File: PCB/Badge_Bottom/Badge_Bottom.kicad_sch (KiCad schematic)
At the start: 10 parts, among them CN1 PJ-320, CN2 PJ-320, J1 USB_C_Receptacle_USB2.0, J3 Conn_01x01_Pin, Q1 AO3400A, SW1 TM-2024A, SW2 TM-2024A, U2 CH32V305RBT6

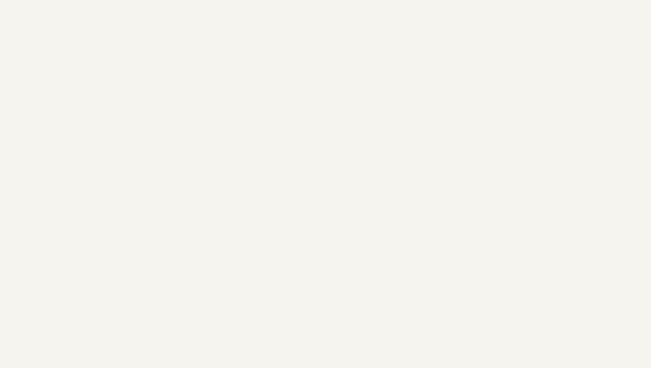
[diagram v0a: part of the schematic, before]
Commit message: Added todo for bottom badge
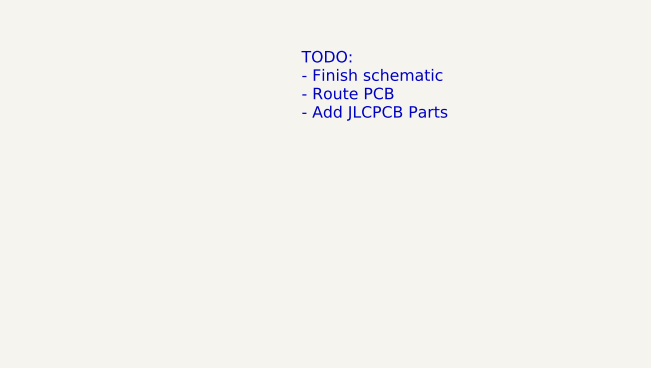
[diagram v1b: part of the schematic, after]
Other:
- note added: "TODO: - Finish schematic - Route PCB - Add JLCPCB Parts"
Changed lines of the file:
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@@
     (stroke (width 0) (type default))
+  )
+  (text "TODO:\n- Finish schematic\n- Route PCB\n- Add JLCPCB Parts"
+    (at 204.47 36.83 0)
+    (effects (font (size 1.27 1.27)) (justify left bottom))
   )
   (symbol (lib_id "Connector:USB_C_Receptacle_USB2.0") (at 50.8 99.06 0) (unit 1)

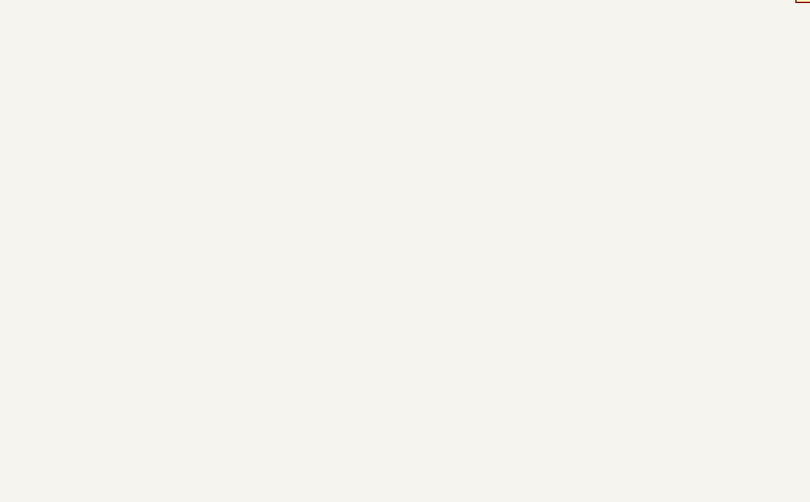
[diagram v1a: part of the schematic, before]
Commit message: Added pcb outline from Badge_Top, added todos in pcb file
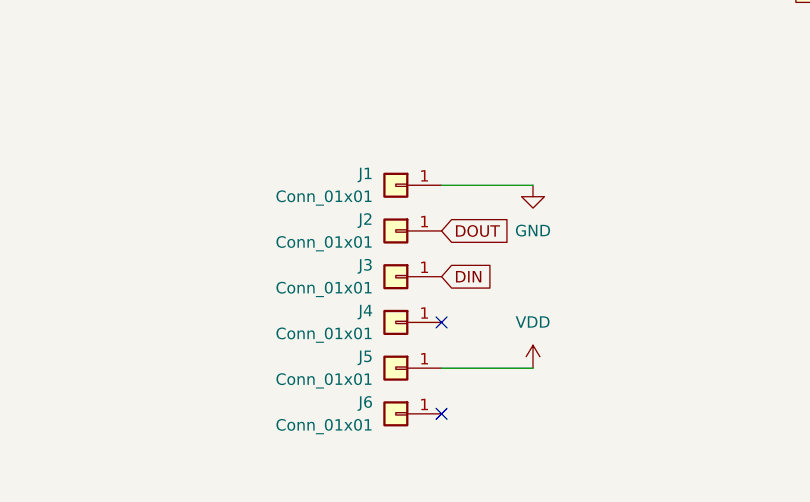
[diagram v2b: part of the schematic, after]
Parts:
- added J1, J2, J3, J4, J5, J6: Conn_01x01, Mounting_Wuerth:Mounting_Wuerth_WA-SMSI-M2_H7mm_9774070243, symbol Connector_Generic:Conn_01x01
- CN1, CN2: footprint kicad:AUDIO-TH_HOOYA_PJ-320 -> PJ-320:AUDIO-TH_HOOYA_PJ-320
- J1: footprint (none) -> Connector_USB:USB_C_Receptacle_HRO_TYPE-C-31-M-12
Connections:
- net GND: now also J1.1 (Pin_1)
- new net DIN: J3.1 (Pin_1)
- new net DOUT: J2.1 (Pin_1)
- new net VDD: J5.1 (Pin_1)
- no-connect marks 0 -> 2

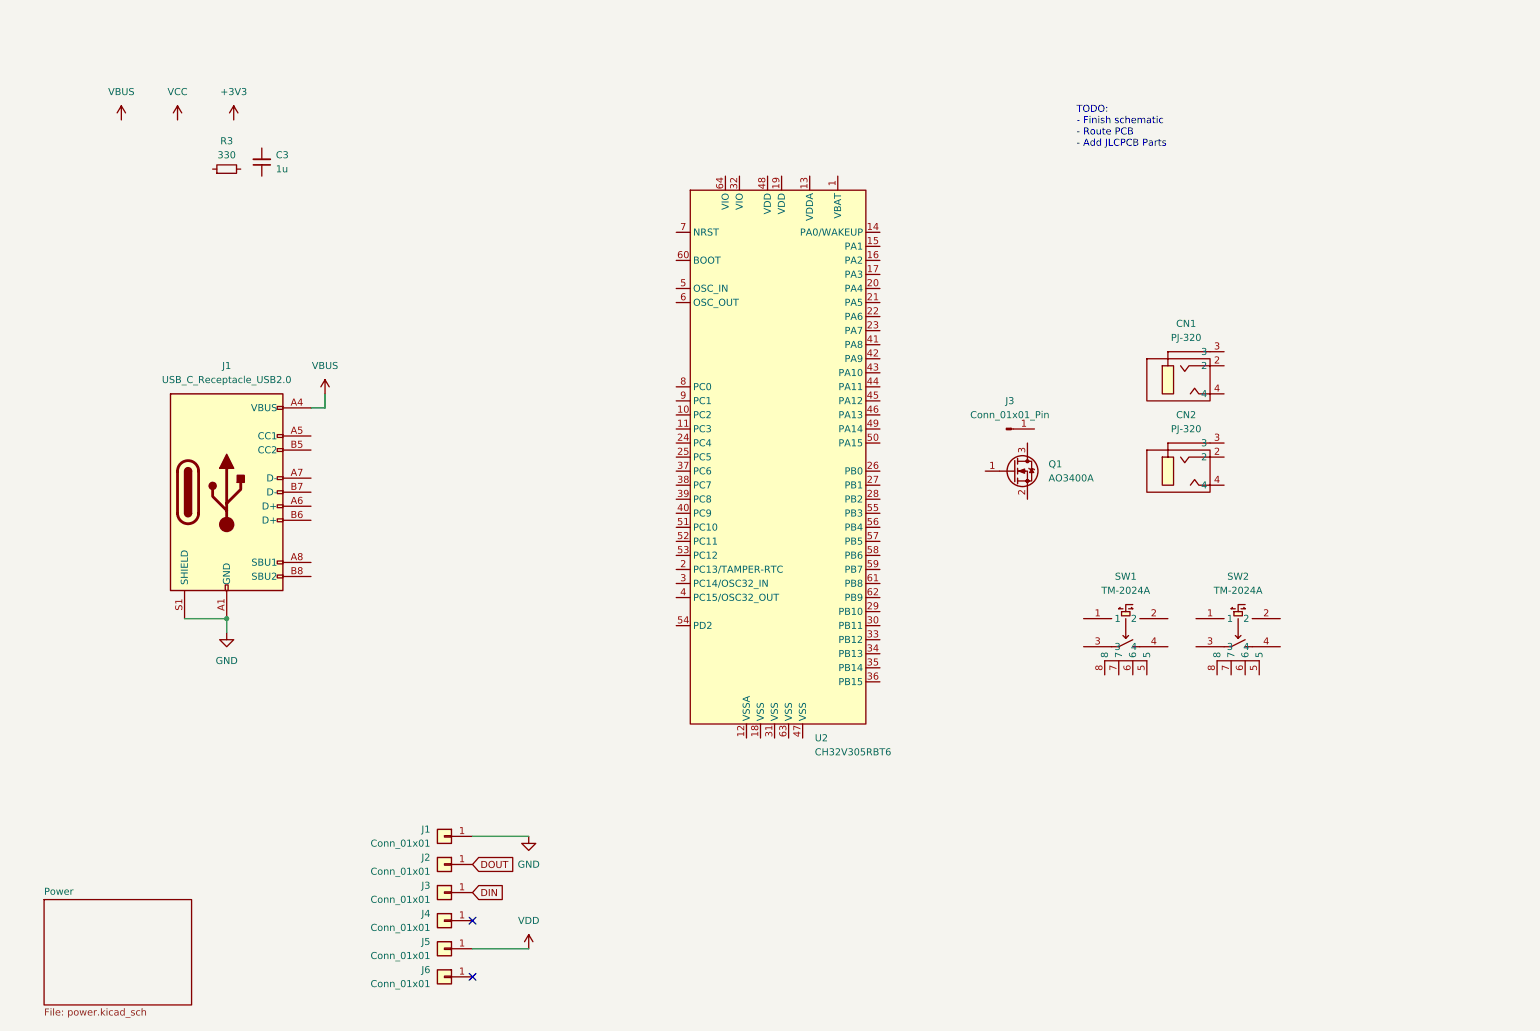
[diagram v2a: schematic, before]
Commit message: Added new page for IO, added new components, added JLC parts, fixed PCB standoffs to be pads and modified concept of PCB (dual usbc)
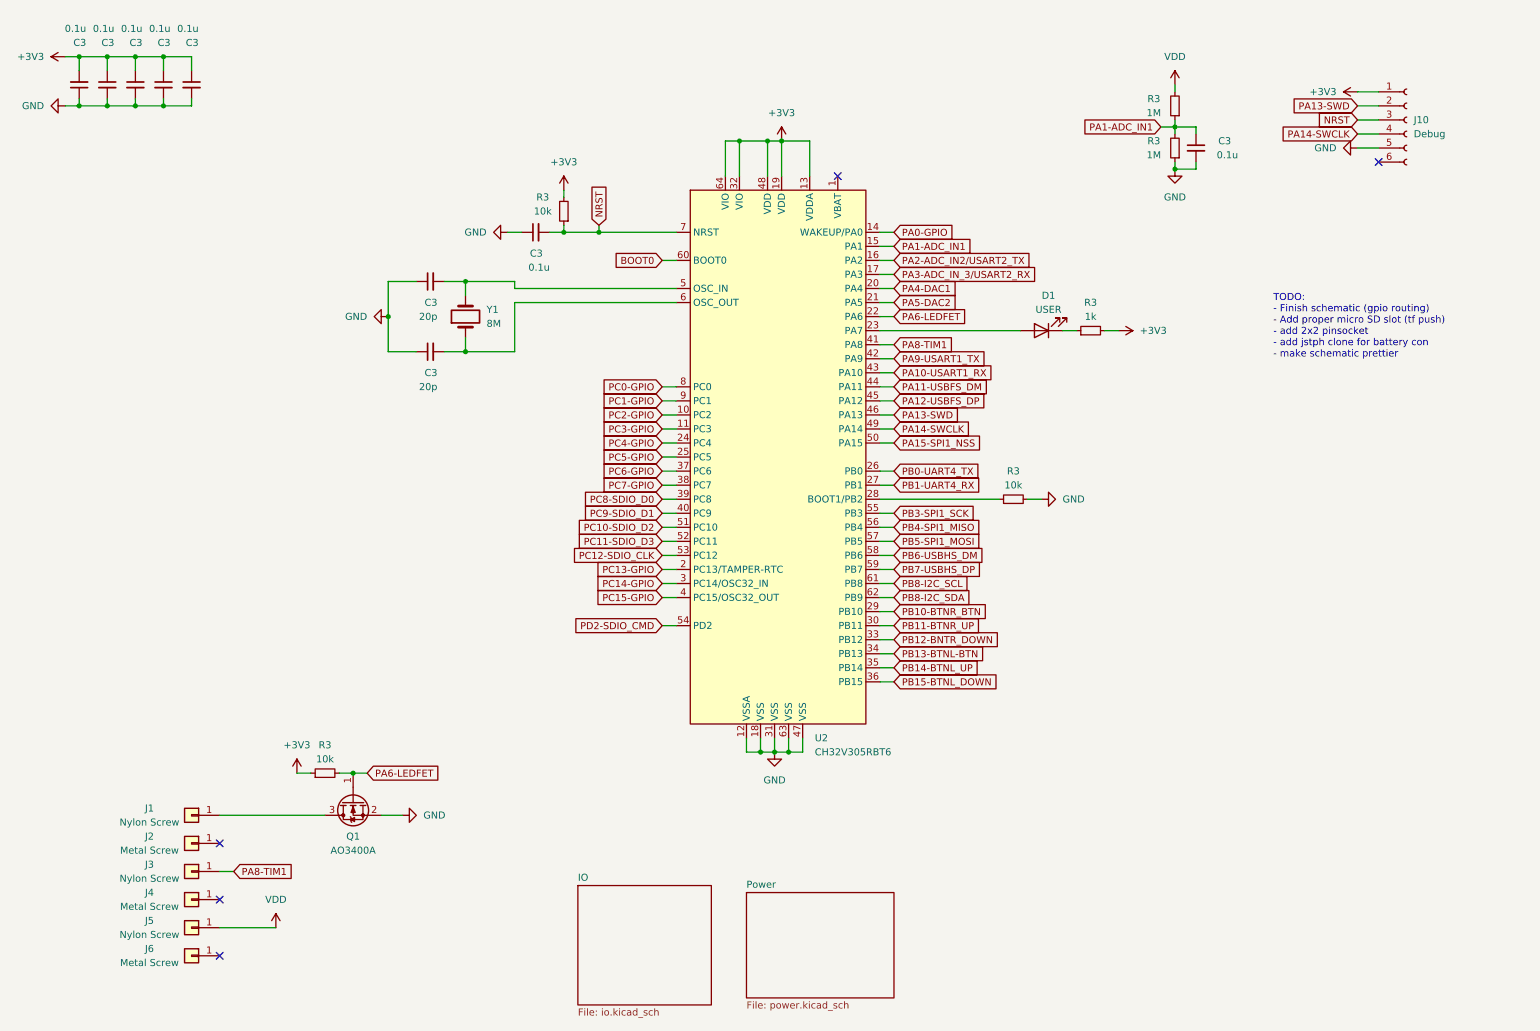
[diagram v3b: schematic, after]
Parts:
- removed CN1, CN2: PJ-320, PJ-320:AUDIO-TH_HOOYA_PJ-320, symbol PJ-320:PJ-320
- removed J1: USB_C_Receptacle_USB2.0, Connector_USB:USB_C_Receptacle_HRO_TYPE-C-31-M-12, symbol Connector:USB_C_Receptacle_USB2.0
- removed J3: Conn_01x01_Pin, Connector_Wire:SolderWirePad_1x01_SMD_1x2mm, symbol Connector:Conn_01x01_Pin
- removed SW1, SW2: TM-2024A, TM2024A:SW-SMD_TM-2024A, symbol TM2024A:TM-2024A
- added C3 (x6): 0.1u, Capacitor_SMD:C_0603_1608Metric, symbol Device:C_Small
- added C3 (x2): 20p, Capacitor_SMD:C_0603_1608Metric, symbol Device:C_Small
- added D1: USER, LED_SMD:LED_0603_1608Metric, symbol Device:LED
- added J10: Debug, Paw-Connect_RevB_TC2030-IDC-NL_2x03_P1.27mm_Vertical:Paw-Connect_RevB_TC2030-IDC-NL_2x03_P1.27mm_Vertical, symbol Connector:Conn_01x06_Socket
- added R3 (x2): 10k, Resistor_SMD:R_0603_1608Metric, symbol Device:R_Small
- added R3 (x2): 1M, Resistor_SMD:R_0603_1608Metric, symbol Device:R_Small
- added R3: 1k, Resistor_SMD:R_0603_1608Metric, symbol Device:R_Small
- added Y1: 8M, Crystal:Crystal_SMD_5032-2Pin_5.0x3.2mm, symbol Device:Crystal
- C3: value 1u -> 0.1u; footprint (none) -> Capacitor_SMD:C_0603_1608Metric
- J1, J3, J5: value Conn_01x01 -> Nylon Screw; footprint Mounting_Wuerth:Mounting_Wuerth_WA-SMSI-M2_H7mm_9774070243 -> standoff_pad_m2:Standoff_Pad_M2
- J2, J4, J6: value Conn_01x01 -> Metal Screw; footprint Mounting_Wuerth:Mounting_Wuerth_WA-SMSI-M2_H7mm_9774070243 -> standoff_pad_m2:Standoff_Pad_M2
- R3: value 330 -> 10k; footprint (none) -> Resistor_SMD:R_0603_1608Metric
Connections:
- net DIN is gone; now on net PA8-TIM1: J3.1 (Pin_1)
- net +3V3: now also C3.1, U2.13 (VDDA), U2.19 (VDD), U2.32 (VIO), U2.48 (VDD), U2.64 (VIO), C3.1, C3.1, C3.1, C3.2, J10.1 (Pin_1), R3.1, R3.2, R3.2
- net GND: now also C3.2, Q1.2 (S), R3.2, U2.12 (VSSA), U2.18 (VSS), U2.31 (VSS), U2.47 (VSS), U2.63 (VSS), C3.1, C3.1, C3.1, C3.1, C3.2, C3.2, C3.2, C3.2, J10.5 (Pin_5), R3.1; no longer J1.1 (Pin_1)
- net VDD: now also R3.2
- net at R3.1: now also U2.28 (BOOT1/PB2)
- net PC2-GPIO: now reaches U2.10 (PC2)
- net PC3-GPIO: now reaches U2.11 (PC3)
- net PA0-GPIO: now reaches U2.14 (WAKEUP/PA0)
- net PA1-ADC_IN1: now reaches U2.15 (PA1)
- net PA1-ADC_IN1: now also C3.1, R3.1, R3.2
- net PA2-ADC_IN2/USART2_TX: now reaches U2.16 (PA2)
- net PA3-ADC_IN_3/USART2_RX: now reaches U2.17 (PA3)
- net PC13-GPIO: now reaches U2.2 (PC13/TAMPER-RTC)
- net PA4-DAC1: now reaches U2.20 (PA4)
- net PA5-DAC2: now reaches U2.21 (PA5)
- net PA6-LEDFET: now reaches U2.22 (PA6)
- net PA6-LEDFET: now also Q1.1 (G), R3.2
- net at U2.23 (PA7): now also D1.2 (A)
- net PC4-GPIO: now reaches U2.24 (PC4)
- net PC5-GPIO: now reaches U2.25 (PC5)
- net PB0-UART4_TX: now reaches U2.26 (PB0)
- net PB1-UART4_RX: now reaches U2.27 (PB1)
- net PB10-BTNR_BTN: now reaches U2.29 (PB10)
- net PC14-GPIO: now reaches U2.3 (PC14/OSC32_IN)
- net PB11-BTNR_UP: now reaches U2.30 (PB11)
- net PB12-BNTR_DOWN: now reaches U2.33 (PB12)
- net PB13-BTNL-BTN: now reaches U2.34 (PB13)
- net PB14-BTNL_UP: now reaches U2.35 (PB14)
- net PB15-BTNL_DOWN: now reaches U2.36 (PB15)
- net PC6-GPIO: now reaches U2.37 (PC6)
- net PC7-GPIO: now reaches U2.38 (PC7)
- net PC8-SDIO_D0: now reaches U2.39 (PC8)
- net PC15-GPIO: now reaches U2.4 (PC15/OSC32_OUT)
- net PC9-SDIO_D1: now reaches U2.40 (PC9)
- net PA8-TIM1: now reaches U2.41 (PA8)
- net PA9-USART1_TX: now reaches U2.42 (PA9)
- net PA10-USART1_RX: now reaches U2.43 (PA10)
- net PA11-USBFS_DM: now reaches U2.44 (PA11)
- net PA12-USBFS_DP: now reaches U2.45 (PA12)
- net PA13-SWD: now reaches U2.46 (PA13)
- net PA13-SWD: now also J10.2 (Pin_2)
- net PA14-SWCLK: now reaches U2.49 (PA14)
- net PA14-SWCLK: now also J10.4 (Pin_4)
- net at U2.5 (OSC_IN): now also C3.2, Y1.2
- net PA15-SPI1_NSS: now reaches U2.50 (PA15)
- net PC10-SDIO_D2: now reaches U2.51 (PC10)
- net PC11-SDIO_D3: now reaches U2.52 (PC11)
- net PC12-SDIO_CLK: now reaches U2.53 (PC12)
- net PD2-SDIO_CMD: now reaches U2.54 (PD2)
- net PB3-SPI1_SCK: now reaches U2.55 (PB3)
- net PB4-SPI1_MISO: now reaches U2.56 (PB4)
- net PB5-SPI1_MOSI: now reaches U2.57 (PB5)
- net PB6-USBHS_DM: now reaches U2.58 (PB6)
- net PB7-USBHS_DP: now reaches U2.59 (PB7)
- net at U2.6 (OSC_OUT): now also C3.2, Y1.1
- net BOOT0: now reaches U2.60 (BOOT0)
- net PB8-I2C_SCL: now reaches U2.61 (PB8)
- net PB8-I2C_SDA: now reaches U2.62 (PB9)
- net NRST: now reaches U2.7 (NRST)
- net NRST: now also C3.2, J10.3 (Pin_3), R3.1
- net PC0-GPIO: now reaches U2.8 (PC0)
- net PC1-GPIO: now reaches U2.9 (PC1)
- net at Q1.3 (D): now also J1.1 (Pin_1)
- net DOUT: no longer names the net of J2.1 (Pin_1)
- new net: D1.1 (K), R3.1
- no-connect marks 2 -> 5
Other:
- added sheet IO (io.kicad_sch)
- note added: "TODO: - Finish schematic (gpio routing) - Add proper micro SD slot (tf push) - add 2x2 pinsocket - add jstph clone for battery con - make schematic prettier"
- note removed: "TODO: - Finish schematic - Route PCB - Add JLCPCB Parts"
- moved on the sheet: C3, J1, J2, J3, J4, J5, J6, Q1, R3

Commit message: finished schematic and added jlc parts
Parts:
- added J18: Debug, Connector_PinSocket_2.54mm:PinSocket_2x02_P2.54mm_Horizontal, symbol Connector_Generic:Conn_02x02_Odd_Even
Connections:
- net GND: now also J18.1 (Pin_1)
- net NRST: now also J18.3 (Pin_3)
- net PA13-SWD: now also J18.2 (Pin_2)
- net PA14-SWCLK: now also J18.4 (Pin_4)
- net PB8-I2C_SDA renamed PB9-I2C_SDA
- net PC13-GPIO renamed PC13-SDIO_CD
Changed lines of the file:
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@@
+    (stroke (width 0) (type default))
+  )
+  (wire (pts (xy 261.62 49.53) (xy 264.16 49.53))
     (stroke (width 0) (type default))
   )
@@
     (stroke (width 0) (type default))
   )
+  (wire (pts (xy 246.38 52.07) (xy 248.92 52.07))
+    (stroke (width 0) (type default))
+  )
   (wire (pts (xy 44.45 29.21) (xy 44.45 27.94))
     (stroke (width 0) (type default))
@@
     (stroke (width 0) (type default))
   )
+  (wire (pts (xy 246.38 49.53) (xy 248.92 49.53))
+    (stroke (width 0) (type default))
+  )
   (wire (pts (xy 21.59 20.32) (xy 24.13 20.32))
     (stroke (width 0) (type default))
@@
   )
   (wire (pts (xy 109.22 52.07) (xy 111.76 52.07))
+    (stroke (width 0) (type default))
+  )
+  (wire (pts (xy 261.62 52.07) (xy 264.16 52.07))
     (stroke (width 0) (type default))
   )
@@
     )
   )
-  (global_label "PB8-I2C_SDA" (shape input) (at 171.45 118.11 0) (fields_autoplaced)
+  (global_label "PB9-I2C_SDA" (shape input) (at 171.45 118.11 0) (fields_autoplaced)
     (effects (font (size 1.27 1.27)) (justify left))
     (property "Intersheetrefs" "${INTERSHEET_REFS}" (at 187.3771 118.11 0)
@@
     )
   )
+  (global_label "NRST" (shape input) (at 246.38 52.07 180) (fields_autoplaced)
+    (effects (font (size 1.27 1.27)) (justify right))
+    (property "Intersheetrefs" "${INTERSHEET_REFS}" (at 238.6172 52.07 0)
+      (effects (font (size 1.27 1.27)) (justify right) hide)
+    )
+  )
   (global_label "PC11-SDIO_D3" (shape input) (at 129.54 107.95 180) (fields_autoplaced)
     (effects (font (size 1.27 1.27)) (justify right))
@@
     )
   )
+  (global_label "PA14-SWCLK" (shape input) (at 264.16 52.07 0) (fields_autoplaced)
+    (effects (font (size 1.27 1.27)) (justify left))
+    (property "Intersheetrefs" "${INTERSHEET_REFS}" (at 279.7242 52.07 0)
+      (effects (font (size 1.27 1.27)) (justify left) hide)
+    )
+  )
   (global_label "PC0-GPIO" (shape input) (at 129.54 80.01 180) (fields_autoplaced)
     (effects (font (size 1.27 1.27)) (justify right))
@@
     )
   )
-  (global_label "PC13-GPIO" (shape input) (at 129.54 113.03 180) (fields_autoplaced)
+  (global_label "PC13-SDIO_CD" (shape input) (at 129.54 113.03 180) (fields_autoplaced)
     (effects (font (size 1.27 1.27)) (justify right))
     (property "Intersheetrefs" "${INTERSHEET_REFS}" (at 115.5481 113.03 0)
@@
     (property "Intersheetrefs" "${INTERSHEET_REFS}" (at 113.371 100.33 0)
       (effects (font (size 1.27 1.27)) (justify right) hide)
+    )
+  )
+  (global_label "PA13-SWD" (shape input) (at 264.16 49.53 0) (fields_autoplaced)
+    (effects (font (size 1.27 1.27)) (justify left))
+    (property "Intersheetrefs" "${INTERSHEET_REFS}" (at 277.4261 49.53 0)
+      (effects (font (size 1.27 1.27)) (justify left) hide)
     )
   )
@@
         (path "/9bea0129-61af-4534-9a88-a88b63234707/0f55777b-99bc-476f-91c2-8f0549bc7bba"
           (reference "#PWR014") (unit 1)
+        )
+      )
+    )
+  )
+  (symbol (lib_id "Connector_Generic:Conn_02x02_Odd_Even") (at 254 49.53 0) (unit 1)
+    (in_bom yes) (on_board yes) (dnp no) (fields_autoplaced)
+    (property "Reference" "J18" (at 255.27 43.18 0)
+      (effects (font (size 1.27 1.27)))
+    )
+    (property "Value" "Debug" (at 255.27 45.72 0)
+      (effects (font (size 1.27 1.27)))
+    )
+    (property "Footprint" "Connector_PinSocket_2.54mm:PinSocket_2x02_P2.54mm_Horizontal" (at 254 49.53 0)
+      (effects (font (size 1.27 1.27)) hide)
+    )
+    (property "Datasheet" "~" (at 254 49.53 0)
+      (effects (font (size 1.27 1.27)) hide)
+    )
+    (pin "1")
+    (pin "2")
+    (pin "3")
+    (pin "4")
+    (instances
+      (project "Badge_Bottom"
+        (path "/9bea0129-61af-4534-9a88-a88b63234707/8d25bc71-ccea-4834-b12f-ddce477db9bd"
+          (reference "J18") (unit 1)
+        )
+        (path "/9bea0129-61af-4534-9a88-a88b63234707"
+          (reference "J20") (unit 1)
         )
       )
@@
         )
       )
+    )
+  )
+  (symbol (lib_id "power:GND") (at 246.38 49.53 270) (unit 1)
+    (in_bom yes) (on_board yes) (dnp no) (fields_autoplaced)
+    (property "Reference" "#PWR055" (at 240.03 49.53 0)
+      (effects (font (size 1.27 1.27)) hide)
+    )
+    (property "Value" "GND" (at 242.57 49.53 90)
+      (effects (font (size 1.27 1.27)) (justify right))
+    )
+    (property "Footprint" "" (at 246.38 49.53 0)
+      (effects (font (size 1.27 1.27)) hide)
+    )
+    (property "Datasheet" "" (at 246.38 49.53 0)
+      (effects (font (size 1.27 1.27)) hide)
+    )
+    (pin "1")
+    (instances
+      (project "Badge_Bottom"
+        (path "/9bea0129-61af-4534-9a88-a88b63234707"
+          (reference "#PWR055") (unit 1)
+        )
+      )
